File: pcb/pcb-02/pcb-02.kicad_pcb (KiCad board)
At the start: 2 copper layers, 24 x 8 mm, 2 parts

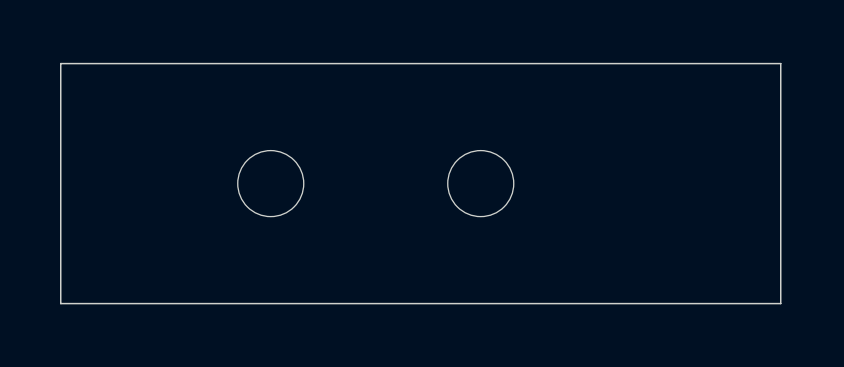
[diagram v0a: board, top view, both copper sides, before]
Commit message: pcb: PCB-02 placed -- ready for routing
U1 (2.5,4) on the magnet sweep centerline at the inner end, C1 at
(2.5,1.3) over U1's VCC/GND pads, J1 rot 90 with the pad row at x 17.7
and the body flush at the outer edge, face off-board. Verified from the
file with board_model (pads, nets, courtyards), headless DRC clean
except the J1 silk-over-edge waivers now baselined in
pcb/pcb-02/placement/waivers.md.

H2 moved (14,4) -> (13,4): with exact courtyards, an M2 washer at 14
would touch the S3B body. electrical.md + project.json carry the new
BR-100 datum.

pcb/tools apply_positions.py, board_model.py, and render_board.sh now
take a STILLAIR_BOARD env override instead of hardcoding pcb-01.

Next: Michael routes the three nets; Claude runs the DRC-diff loop.
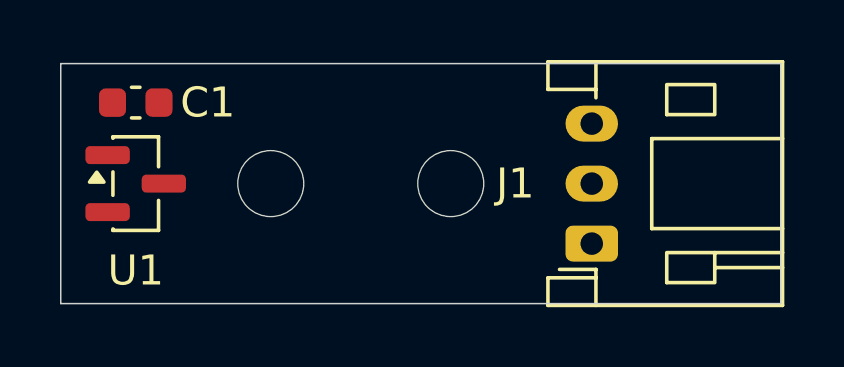
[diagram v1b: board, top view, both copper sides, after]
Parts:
- added C1: 100nF, Capacitor_SMD:C_0603_1608Metric, F.Cu at (52.5, 51.3)
- added J1: HALL_TO_J3, Connector_JST:JST_PH_S3B-PH-K_1x03_P2.00mm_Horizontal, F.Cu at (67.7, 56.0)
- added U1: DRV5033FAQDBZR, Package_TO_SOT_SMD:SOT-23, F.Cu at (52.5, 54.0)
- moved H2 1.00 mm to (63.0, 54.0)

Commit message: pcb: PCB-02 routed clean + board-truth review swarm integrated
Michael routed the three nets (3V3 north, HALL_TACH south, AGND on a
B.Cu pour); headless DRC sits exactly at the waivers baseline: 8 J1
silk-over-edge warnings, 0 unconnected.

Four-agent review swarm (pin functions, system path, placement physics,
completeness critic) against board-extracted artifacts with docs
off-limits: every pad-to-function mapping verified from TI/JST primary
documents, the full sensor-to-LM2907 chain traced across both boards,
no hidden cable reversal between the side-entry and top-entry PH
headers. No board changes survived triage; findings landed as docs:

- Gap datum defined: measured to the SOT-23's marked face; the Hall
  element sits ~0.4 mm behind it (electrical.md, parts.md).
- BR-100 handoff: J1 is the tallest rotor-facing feature, bracket owns
  strain relief, H1 washer <=O4.5 (electrical.md, parts.md, waivers.md).
- TACH-06 harness continuity check added to the test matrix (both cable
  ends are hand-crimped; a swapped contact is a silently dead tach).
- Series R on HALL_TACH considered and declined, rationale recorded.
- Omnipolar clarification: south-pole magnet orientation is convention,
  not assembly-critical.

Next: generalize pcb/tools/jlc_fab.py and build the fab package.
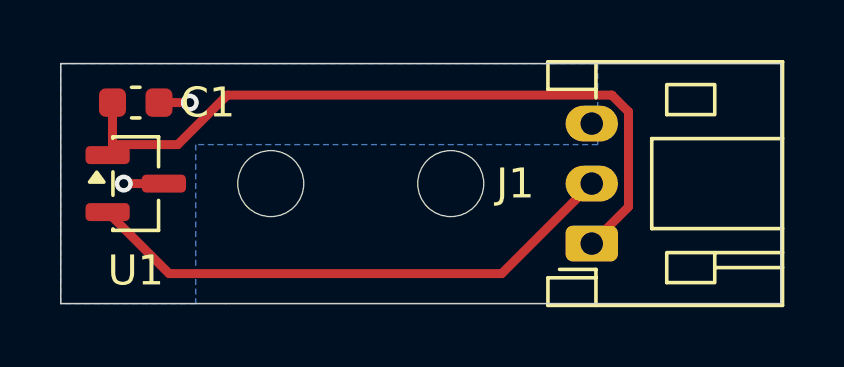
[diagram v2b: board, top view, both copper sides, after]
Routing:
- net /3V3: track 0.00 -> 24.8 mm
- net /HALL_TACH: track 0.00 -> 18.2 mm
- net /AGND: track 0.00 -> 2.36 mm, vias 0 -> 2
- added copper zone on B.Cu, net /AGND
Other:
- outline, holes or cut-outs redrawn

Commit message: pcb: PCB-02 back-silk legend + J1 sourcing to DigiKey
B.SilkS gains the board ID and a per-pin J1 legend (1 3V3 / 2 TACH /
3 GND) readable from the back -- the side that faces up once the board
mounts component-side-down, so it labels the probe points on the
installed board. Konnect's add_board_text writes valid KiCad 10 text
but omits (justify mirror) on back layers; patched by script, quirk
recorded in the /pcb skill. DRC still exactly at the waivers baseline.

S3B-PH-K-S sourcing switched from LCSC-with-board-order to the next
DigiKey order (with C34 + the 100 nF strip): in stock ships-today,
genuine, consolidates shipping, and PCB-02 is a bare-board order so
nothing rides with the fab anyway. The LCSC-at-order-time TODO dies.
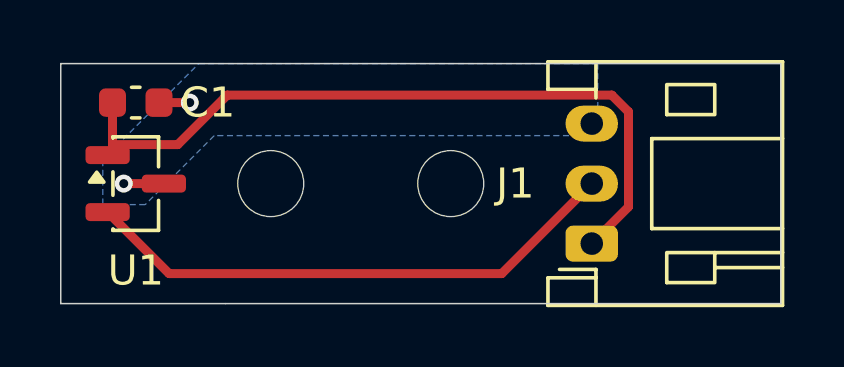
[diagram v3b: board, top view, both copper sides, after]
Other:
- board text added: "1 3V3"
- board text added: "2 TACH"
- board text added: "3 GND"
- board text added: "STILLAIR PCB-02"
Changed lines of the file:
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@@
 		(polygon
 			(pts
-				(xy 50 50) (xy 67.9 50) (xy 67.9 52.7) (xy 54.5 52.7) (xy 54.5 58) (xy 50 58)
+				(xy 51.4 53.2) (xy 54.6 50) (xy 67.9 50) (xy 67.9 52.4) (xy 55.11716 52.4) (xy 52.81716 54.7) (xy 51.4 54.7)
 			)
 		)
 	)
 	(embedded_fonts no)
-)
+  (gr_text "STILLAIR PCB-02"
+    (at 58 56.5 0)
+    (layer "B.SilkS")
+    (effects (font (size 0.8 0.8) (thickness 0.15)) (justify mirror))
+  )
+  (gr_text "1 3V3"
+    (at 70.9 56 0)
+    (layer "B.SilkS")
+    (effects (font (size 0.8 0.8) (thickness 0.15)) (justify mirror))
+  )
+  (gr_text "2 TACH"
+    (at 70.9 54 0)
+    (layer "B.SilkS")
+    (effects (font (size 0.8 0.8) (thickness 0.15)) (justify mirror))
+  )
+  (gr_text "3 GND"
+    (at 70.9 52 0)
+    (layer "B.SilkS")
+    (effects (font (size 0.8 0.8) (thickness 0.15)) (justify mirror))
+  ))
